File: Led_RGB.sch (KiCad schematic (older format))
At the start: 10 parts, among them Q6 BC547, Q7 BC547, Q8 BC547

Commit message: añaadido zocalo para sensor de temperatura y primera distribucion sobre la PCB
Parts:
- removed Q6, Q7, Q8: BC547, Transistors:TO-92_EnLinea_Estrecho_Oval, symbol BC547
- added Q6, Q7, Q8: BC846B, TO_SOT_Packages_SMD:SOT-23, symbol BC849
- R13, R14, R15, R16, R17, R18: footprint Resistencias:Resistencia_1_4_W_10_mm -> Resistors_SMD:R_0805
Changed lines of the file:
@@
 $Descr A4 11693 8268
 encoding utf-8
-Sheet 5 13
+Sheet 5 14
 Title ""
 Date ""
@@
 F 0 "R16" V 5630 3050 50  0000 C CNN
 F 1 "100" V 5550 3050 50  0000 C CNN
-F 2 "Resistencias:Resistencia_1_4_W_10_mm" V 5480 3050 50  0001 C CNN
+F 2 "Resistors_SMD:R_0805" V 5480 3050 50  0001 C CNN
 F 3 "" H 5550 3050 50  0000 C CNN
 F 4 "SR PASSIVES" H 5550 3050 60  0001 C CNN "Fabricante"
@@
 $EndComp
 $Comp
-L BC547 Q6
-U 1 1 5793DB47
-P 5200 3850
-F 0 "Q6" H 5400 3925 50  0000 L CNN
-F 1 "BC547" H 5400 3850 50  0000 L CNN
-F 2 "Transistors:TO-92_EnLinea_Estrecho_Oval" H 5400 3775 50  0001 L CIN
-F 3 "" H 5200 3850 50  0000 L CNN
-F 4 "DIOTEC SEMICONDUCTOR" H 5200 3850 60  0001 C CNN "Fabricante"
-F 5 "BC547CBK" H 5200 3850 60  0001 C CNN "Ref"
-F 6 "500mW" H 5200 3850 60  0001 C CNN "Potencia"
-F 7 "~" H 5200 3850 60  0001 C CNN "Tolerancia"
-F 8 "tme" H 5200 3850 60  0001 C CNN "Provedor"
-F 9 "BC547CBK-DIO" H 5200 3850 60  0001 C CNN "Ref_Proveedor"
-	1    5200 3850
-	1    0    0    -1
-$EndComp
-$Comp
 L R R13
 U 1 1 5793DB54
@@
 F 0 "R13" V 4780 3850 50  0000 C CNN
 F 1 "4K7" V 4700 3850 50  0000 C CNN
-F 2 "Resistencias:Resistencia_1_4_W_10_mm" V 4630 3850 50  0001 C CNN
+F 2 "Resistors_SMD:R_0805" V 4630 3850 50  0001 C CNN
 F 3 "" H 4700 3850 50  0000 C CNN
 F 4 "~" H 4700 3850 60  0001 C CNN "Fabricante"
@@
 F 0 "R14" V 4780 4250 50  0000 C CNN
 F 1 "4K7" V 4700 4250 50  0000 C CNN
-F 2 "Resistencias:Resistencia_1_4_W_10_mm" V 4630 4250 50  0001 C CNN
+F 2 "Resistors_SMD:R_0805" V 4630 4250 50  0001 C CNN
 F 3 "" H 4700 4250 50  0000 C CNN
 	1    4700 4250
@@
 F 0 "R15" V 4780 4650 50  0000 C CNN
 F 1 "4K7" V 4700 4650 50  0000 C CNN
-F 2 "Resistencias:Resistencia_1_4_W_10_mm" V 4630 4650 50  0001 C CNN
+F 2 "Resistors_SMD:R_0805" V 4630 4650 50  0001 C CNN
 F 3 "" H 4700 4650 50  0000 C CNN
 F 4 "~" H 4700 4650 60  0001 C CNN "Fabricante"
@@
 $EndComp
 $Comp
-L BC547 Q7
-U 1 1 5793DB75
-P 5650 4250
-F 0 "Q7" H 5850 4325 50  0000 L CNN
-F 1 "BC547" H 5850 4250 50  0000 L CNN
-F 2 "Transistors:TO-92_EnLinea_Estrecho_Oval" H 5850 4175 50  0001 L CIN
-F 3 "" H 5650 4250 50  0000 L CNN
-F 4 "DIOTEC SEMICONDUCTOR" H 5650 4250 60  0001 C CNN "Fabricante"
-F 5 "BC547CBK" H 5650 4250 60  0001 C CNN "Ref"
-F 6 "500mW" H 5650 4250 60  0001 C CNN "Potencia"
-F 7 "~" H 5650 4250 60  0001 C CNN "Tolerancia"
-F 8 "tme" H 5650 4250 60  0001 C CNN "Provedor"
-F 9 "BC547CBK-DIO" H 5650 4250 60  0001 C CNN "Ref_Proveedor"
-	1    5650 4250
-	1    0    0    -1
-$EndComp
-$Comp
-L BC547 Q8
-U 1 1 5793DB82
-P 6100 4650
-F 0 "Q8" H 6300 4725 50  0000 L CNN
-F 1 "BC547" H 6300 4650 50  0000 L CNN
-F 2 "Transistors:TO-92_EnLinea_Estrecho_Oval" H 6300 4575 50  0001 L CIN
-F 3 "" H 6100 4650 50  0000 L CNN
-F 4 "DIOTEC SEMICONDUCTOR" H 6100 4650 60  0001 C CNN "Fabricante"
-F 5 "BC547CBK" H 6100 4650 60  0001 C CNN "Ref"
-F 6 "500mW" H 6100 4650 60  0001 C CNN "Potencia"
-F 7 "~" H 6100 4650 60  0001 C CNN "Tolerancia"
-F 8 "tme" H 6100 4650 60  0001 C CNN "Provedor"
-F 9 "BC547CBK-DIO" H 6100 4650 60  0001 C CNN "Ref_Proveedor"
-	1    6100 4650
-	1    0    0    -1
-$EndComp
-$Comp
 L +5V #PWR017
 U 1 1 5793DB89
@@
 F 0 "R17" V 5830 3050 50  0000 C CNN
 F 1 "100" V 5750 3050 50  0000 C CNN
-F 2 "Resistencias:Resistencia_1_4_W_10_mm" V 5680 3050 50  0001 C CNN
+F 2 "Resistors_SMD:R_0805" V 5680 3050 50  0001 C CNN
 F 3 "" H 5750 3050 50  0000 C CNN
 F 4 "SR PASSIVES" H 5750 3050 60  0001 C CNN "Fabricante"
@@
 F 0 "R18" V 6030 3050 50  0000 C CNN
 F 1 "100" V 5950 3050 50  0000 C CNN
-F 2 "Resistencias:Resistencia_1_4_W_10_mm" V 5880 3050 50  0001 C CNN
+F 2 "Resistors_SMD:R_0805" V 5880 3050 50  0001 C CNN
 F 3 "" H 5950 3050 50  0000 C CNN
 F 4 "SR PASSIVES" H 5950 3050 60  0001 C CNN "Fabricante"
@@
 Text GLabel 4050 4650 0    60   Input ~ 0
 D11
+$Comp
+L BC849 Q6
+U 1 1 5797EAC9
+P 5200 3850
+F 0 "Q6" H 5391 3896 50  0000 L CNN
+F 1 "BC846B" H 5391 3805 50  0000 L CNN
+F 2 "TO_SOT_Packages_SMD:SOT-23" H 5391 3759 50  0001 L CIN
+F 3 "http://www.tme.eu/es/Document/f91a62334f0250ffe02449626443b5d1/BC846_BC546_SER.pdf" H 5391 3759 50  0001 L CNN
+F 4 "nxp" H 5200 3850 60  0001 C CNN "Fabricante"
+F 5 "BC846B.215" H 5200 3850 60  0001 C CNN "Ref"
+F 6 "~" H 5200 3850 60  0001 C CNN "Potencia"
+F 7 "~" H 5200 3850 60  0001 C CNN "Tolerancia"
+F 8 "tme" H 5200 3850 60  0001 C CNN "Provedor"
+F 9 "BC846B.215" H 5200 3850 60  0001 C CNN "Ref_Proveedor"
+	1    5200 3850
+	1    0    0    -1
+$EndComp
+$Comp
+L BC849 Q7
+U 1 1 5797ECAC
+P 5650 4250
+F 0 "Q7" H 5841 4296 50  0000 L CNN
+F 1 "BC846B" H 5841 4205 50  0000 L CNN
+F 2 "TO_SOT_Packages_SMD:SOT-23" H 5841 4159 50  0001 L CIN
+F 3 "http://www.tme.eu/es/Document/f91a62334f0250ffe02449626443b5d1/BC846_BC546_SER.pdf" H 5841 4159 50  0001 L CNN
+F 4 "nxp" H 5650 4250 60  0001 C CNN "Fabricante"
+F 5 "BC846B.215" H 5650 4250 60  0001 C CNN "Ref"
+F 6 "~" H 5650 4250 60  0001 C CNN "Potencia"
+F 7 "~" H 5650 4250 60  0001 C CNN "Tolerancia"
+F 8 "tme" H 5650 4250 60  0001 C CNN "Provedor"
+F 9 "BC846B.215" H 5650 4250 60  0001 C CNN "Ref_Proveedor"
+	1    5650 4250
+	1    0    0    -1
+$EndComp
+$Comp
+L BC849 Q8
+U 1 1 5797ED07
+P 6100 4650
+F 0 "Q8" H 6291 4696 50  0000 L CNN
+F 1 "BC846B" H 6291 4605 50  0000 L CNN
+F 2 "TO_SOT_Packages_SMD:SOT-23" H 6291 4559 50  0001 L CIN
+F 3 "http://www.tme.eu/es/Document/f91a62334f0250ffe02449626443b5d1/BC846_BC546_SER.pdf" H 6291 4559 50  0001 L CNN
+F 4 "nxp" H 6100 4650 60  0001 C CNN "Fabricante"
+F 5 "BC846B.215" H 6100 4650 60  0001 C CNN "Ref"
+F 6 "~" H 6100 4650 60  0001 C CNN "Potencia"
+F 7 "~" H 6100 4650 60  0001 C CNN "Tolerancia"
+F 8 "tme" H 6100 4650 60  0001 C CNN "Provedor"
+F 9 "BC846B.215" H 6100 4650 60  0001 C CNN "Ref_Proveedor"
+	1    6100 4650
+	1    0    0    -1
+$EndComp
 $EndSCHEMATC

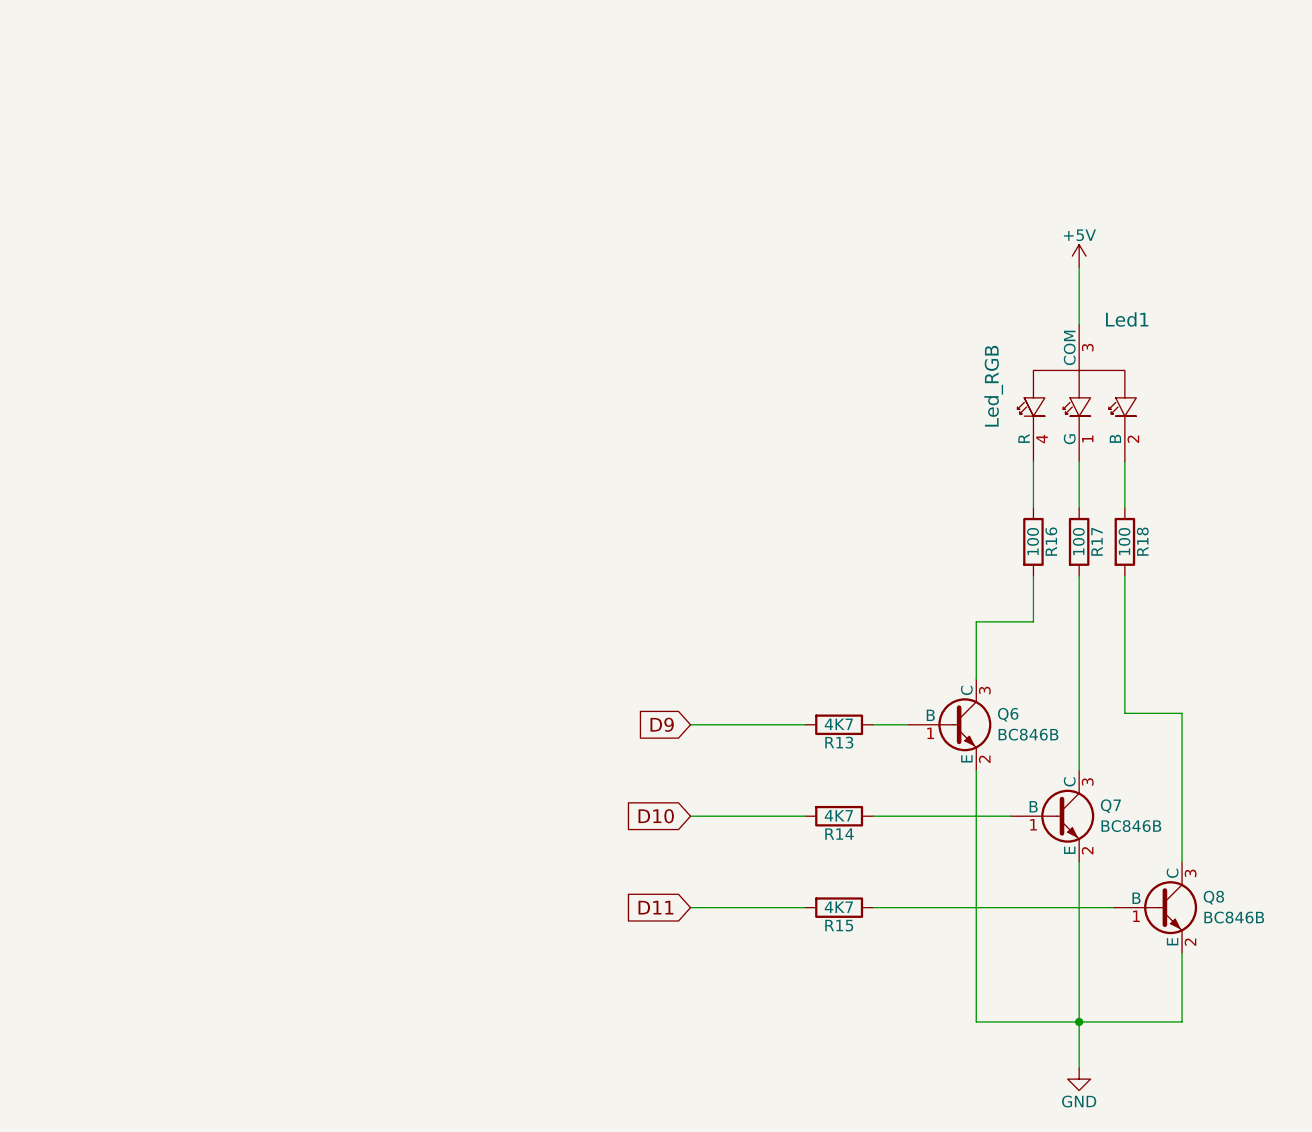
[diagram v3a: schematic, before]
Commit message: ordenar referencias de componentes
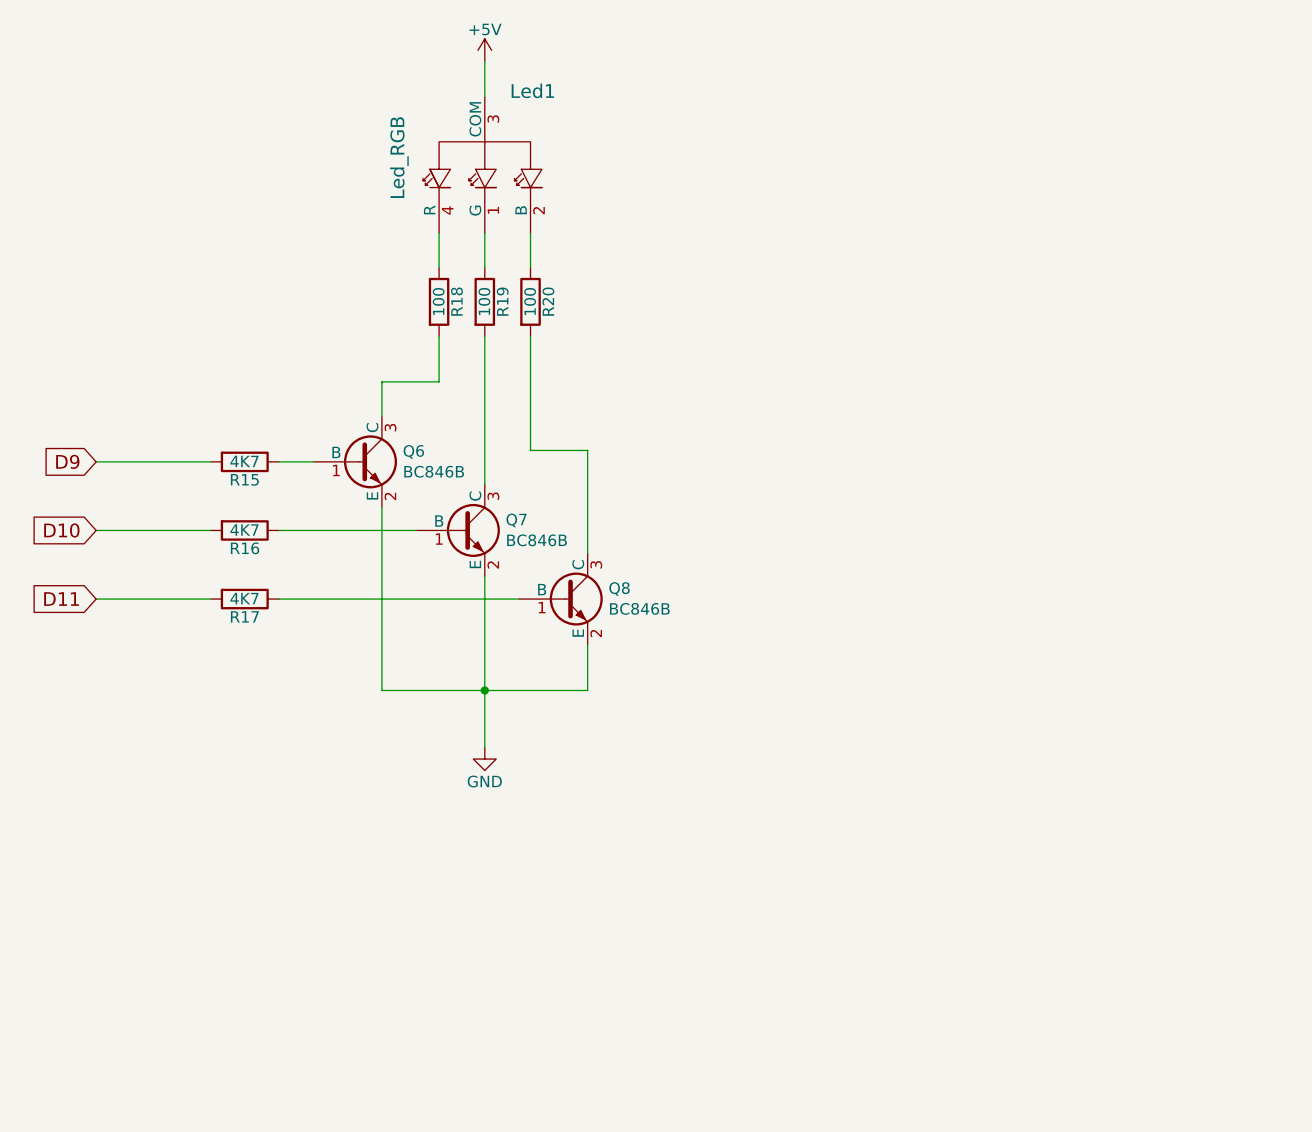
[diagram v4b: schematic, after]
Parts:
- R15: renamed from R13; Fabricante (none) -> VISHAY; Potencia (none) -> 1/8W; Provedor (none) -> TME; Ref (none) -> CRCW08054K70FKEA; Ref_Proveedor (none) -> CRCW08054K70FKEA; Tolerancia (none) -> 1%
- R16: renamed from R14; Fabricante (none) -> VISHAY; Potencia (none) -> 1/8W; Provedor (none) -> TME; Ref (none) -> CRCW08054K70FKEA; Ref_Proveedor (none) -> CRCW08054K70FKEA; Tolerancia (none) -> 1%
- R17: renamed from R15; Fabricante (none) -> VISHAY; Potencia (none) -> 1/8W; Provedor (none) -> TME; Ref (none) -> CRCW08054K70FKEA; Ref_Proveedor (none) -> CRCW08054K70FKEA; Tolerancia (none) -> 1%
- R18: renamed from R16; Fabricante SR PASSIVES -> VISHAY; Potencia 1/4W -> 1/8W; Tolerancia 5% -> 1%
- R19: renamed from R17; Potencia 1/4W -> 1/8W; Tolerancia 5% -> 1%
- R20: renamed from R18; Potencia 1/4W -> 1/8W; Tolerancia 5% -> 1%
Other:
- moved on the sheet: Led1, Q6, Q7, Q8, R15, R16, R17, R18, R19, R20

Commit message: cambiados encoder y potenciometro
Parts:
- R15, R16, R17, R18, R19, R20: footprint Resistors_SMD:R_0805 -> Resistencias:R_0805
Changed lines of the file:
@@
 F 0 "R18" V 3030 2000 50  0000 C CNN
 F 1 "100" V 2950 2000 50  0000 C CNN
-F 2 "Resistors_SMD:R_0805" V 2880 2000 50  0001 C CNN
+F 2 "Resistencias:R_0805" V 2880 2000 50  0001 C CNN
 F 3 "" H 2950 2000 50  0000 C CNN
 F 4 "VISHAY" H 2950 2000 60  0001 C CNN "Fabricante"
@@
 F 0 "R15" V 2180 2700 50  0000 C CNN
 F 1 "4K7" V 2100 2700 50  0000 C CNN
-F 2 "Resistors_SMD:R_0805" V 2030 2700 50  0001 C CNN
+F 2 "Resistencias:R_0805" V 2030 2700 50  0001 C CNN
 F 3 "" H 2100 2700 50  0000 C CNN
 F 4 "VISHAY" H 2100 2700 60  0001 C CNN "Fabricante"
@@
 F 0 "R16" V 2180 3000 50  0000 C CNN
 F 1 "4K7" V 2100 3000 50  0000 C CNN
-F 2 "Resistors_SMD:R_0805" V 2030 3000 50  0001 C CNN
+F 2 "Resistencias:R_0805" V 2030 3000 50  0001 C CNN
 F 3 "" H 2100 3000 50  0000 C CNN
 F 4 "VISHAY" H 2100 2700 60  0001 C CNN "Fabricante"
@@
 F 0 "R17" V 2180 3300 50  0000 C CNN
 F 1 "4K7" V 2100 3300 50  0000 C CNN
-F 2 "Resistors_SMD:R_0805" V 2030 3300 50  0001 C CNN
+F 2 "Resistencias:R_0805" V 2030 3300 50  0001 C CNN
 F 3 "" H 2100 3300 50  0000 C CNN
 F 4 "VISHAY" H 2100 2700 60  0001 C CNN "Fabricante"
@@
 $EndComp
 $Comp
-L +5V #PWR20
+L +5V #PWR022
 U 1 1 5793DB89
 P 3150 950
-F 0 "#PWR20" H 3150 800 50  0001 C CNN
+F 0 "#PWR022" H 3150 800 50  0001 C CNN
 F 1 "+5V" H 3150 1090 50  0000 C CNN
 F 2 "" H 3150 950 50  0000 C CNN
@@
 $EndComp
 $Comp
-L GND #PWR21
+L GND #PWR023
 U 1 1 5793DB8F
 P 3150 3950
-F 0 "#PWR21" H 3150 3700 50  0001 C CNN
+F 0 "#PWR023" H 3150 3700 50  0001 C CNN
 F 1 "GND" H 3150 3800 50  0000 C CNN
 F 2 "" H 3150 3950 50  0000 C CNN
@@
 F 0 "R19" V 3230 2000 50  0000 C CNN
 F 1 "100" V 3150 2000 50  0000 C CNN
-F 2 "Resistors_SMD:R_0805" V 3080 2000 50  0001 C CNN
+F 2 "Resistencias:R_0805" V 3080 2000 50  0001 C CNN
 F 3 "" H 3150 2000 50  0000 C CNN
 F 4 "SR PASSIVES" H 3150 2000 60  0001 C CNN "Fabricante"
@@
 F 0 "R20" V 3430 2000 50  0000 C CNN
 F 1 "100" V 3350 2000 50  0000 C CNN
-F 2 "Resistors_SMD:R_0805" V 3280 2000 50  0001 C CNN
+F 2 "Resistencias:R_0805" V 3280 2000 50  0001 C CNN
 F 3 "" H 3350 2000 50  0000 C CNN
 F 4 "SR PASSIVES" H 3350 2000 60  0001 C CNN "Fabricante"

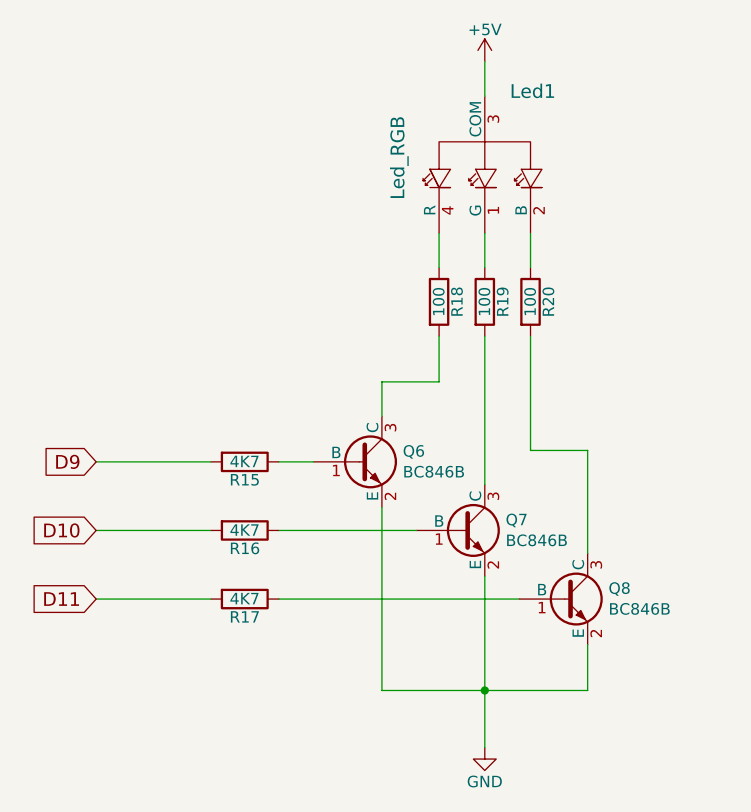
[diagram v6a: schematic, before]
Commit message: añadidos driver para led y conectores para fotodiodos infrarrojos
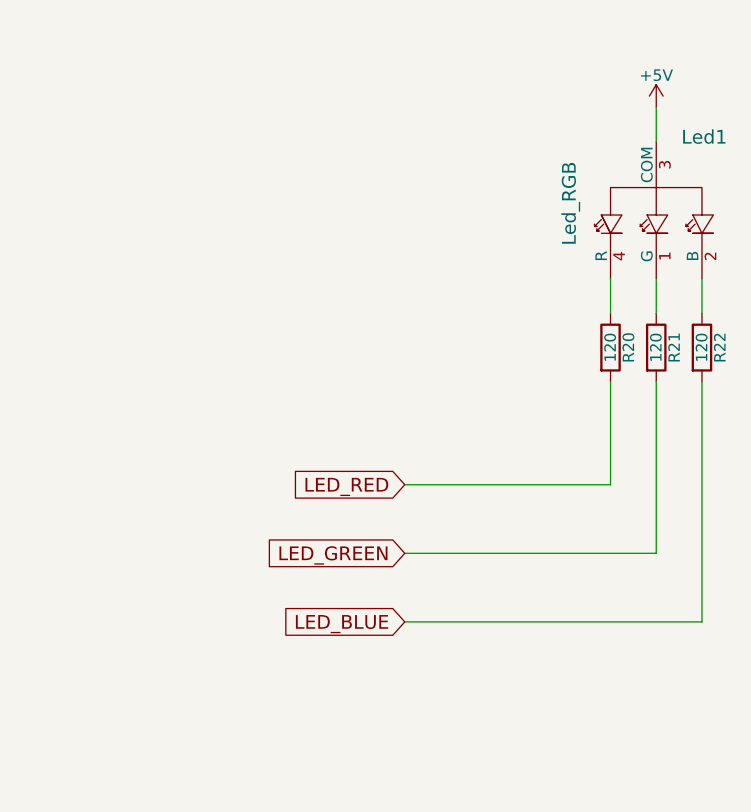
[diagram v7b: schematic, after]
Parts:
- removed Q6, Q7, Q8: BC846B, TO_SOT_Packages_SMD:SOT-23, symbol BC849
- removed R15, R16, R17: 4K7, Resistencias:R_0805, symbol R
- removed R18, R19: 100, Resistencias:R_0805, symbol R
- added R21, R22: 120, Resistencias:R_0805, symbol R
- R20: value 100 -> 120; Fabricante SR PASSIVES -> VISHAY; Ref CF1/4W-100R -> CRCW0805120RFKTABC; Ref_Proveedor CF1/4W-100R -> CRCW0805120RFKTABC
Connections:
- net at Led1.4 (R): now also R20.1
- net at Led1.1 (G): now also R21.1
- net at Led1.2 (B): now also R22.1; no longer R20.1
- net LED_RED: now reaches R20.2
- new net LED_BLUE: R22.2
- new net LED_GREEN: R21.2
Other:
- moved on the sheet: Led1
